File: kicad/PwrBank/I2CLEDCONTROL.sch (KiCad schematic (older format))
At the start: 3 parts, among them U3 PCA9632DP1

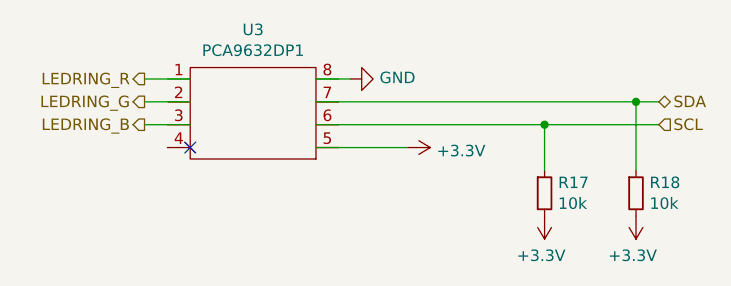
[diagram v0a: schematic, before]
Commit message: Work on schematic+implement capacitive feature using TOUCH0
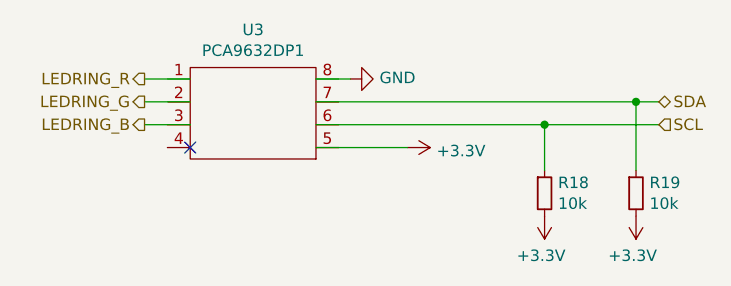
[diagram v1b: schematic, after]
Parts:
- renumbered R17 to R18, R18 to R19
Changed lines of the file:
@@
 LEDRING_B
 $Comp
-L power:GND #PWR034
+L power:GND #PWR036
 U 1 1 60FA879A
 P 4800 3300
-F 0 "#PWR034" H 4800 3050 50  0001 C CNN
+F 0 "#PWR036" H 4800 3050 50  0001 C CNN
 F 1 "GND" V 4805 3172 50  0000 R CNN
 F 2 "" H 4800 3300 50  0001 C CNN
@@
 $EndComp
 $Comp
-L power:+3.3V #PWR035
+L power:+3.3V #PWR037
 U 1 1 60FA900F
 P 5050 3600
-F 0 "#PWR035" H 5050 3450 50  0001 C CNN
+F 0 "#PWR037" H 5050 3450 50  0001 C CNN
 F 1 "+3.3V" V 5065 3728 50  0000 L CNN
 F 2 "" H 5050 3600 50  0001 C CNN
@@
 	4650 3600 5050 3600
 $Comp
-L Device:R_Small R18
+L Device:R_Small R19
 U 1 1 60FAADB1
 P 6050 3800
-F 0 "R18" H 6109 3846 50  0000 L CNN
+F 0 "R19" H 6109 3846 50  0000 L CNN
 F 1 "10k" H 6109 3755 50  0000 L CNN
 F 2 "Resistor_SMD:R_0805_2012Metric_Pad1.20x1.40mm_HandSolder" H 6050 3800 50  0001 C CNN
@@
 	4650 3500 5650 3500
 $Comp
-L Device:R_Small R17
+L Device:R_Small R18
 U 1 1 60FAD892
 P 5650 3800
-F 0 "R17" H 5709 3846 50  0000 L CNN
+F 0 "R18" H 5709 3846 50  0000 L CNN
 F 1 "10k" H 5709 3755 50  0000 L CNN
 F 2 "Resistor_SMD:R_0805_2012Metric_Pad1.20x1.40mm_HandSolder" H 5650 3800 50  0001 C CNN
@@
 	5650 3500 6150 3500
 $Comp
-L power:+3.3V #PWR036
+L power:+3.3V #PWR038
 U 1 1 60FAE153
 P 5650 3900
-F 0 "#PWR036" H 5650 3750 50  0001 C CNN
+F 0 "#PWR038" H 5650 3750 50  0001 C CNN
 F 1 "+3.3V" H 5665 4073 50  0000 C CNN
 F 2 "" H 5650 3900 50  0001 C CNN
@@
 $EndComp
 $Comp
-L power:+3.3V #PWR037
+L power:+3.3V #PWR039
 U 1 1 60FAE9C5
 P 6050 3900
-F 0 "#PWR037" H 6050 3750 50  0001 C CNN
+F 0 "#PWR039" H 6050 3750 50  0001 C CNN
 F 1 "+3.3V" H 6065 4073 50  0000 C CNN
 F 2 "" H 6050 3900 50  0001 C CNN
